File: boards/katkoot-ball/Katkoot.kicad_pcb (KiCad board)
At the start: 2 copper layers, 77.4 x 81.7 mm, 29 parts, among them SW1 Rotary_Encoder_Switch, SW2 SW_Push, SW3 SW_Push, SW5 SW_Push, SW6 SW_Push, SW8 SW_Push, U1 TCR2EF19,LM(CT, U2 PMW3360DM-T2QU, U3 xiao-ble

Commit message: katkoot
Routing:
- net ENC_R: track 101.1 -> 99.7 mm
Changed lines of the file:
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@@
   (segment (start 186.795 39.345) (end 185.23 37.78) (width 0.25) (layer "F.Cu") (net 18))
   (segment (start 187.3 98.85) (end 186.795 98.345) (width 0.25) (layer "F.Cu") (net 18))
-  (segment (start 200.475 107.748833) (end 200.475 106.651167) (width 0.25) (layer "F.Cu") (net 19))
-  (segment (start 199.4 110.95) (end 201.75 108.6) (width 0.25) (layer "F.Cu") (net 19))
-  (segment (start 201.75 108.525) (end 201.251167 108.525) (width 0.25) (layer "F.Cu") (net 19))
-  (segment (start 200.475 106.651167) (end 201.75 105.376167) (width 0.25) (layer "F.Cu") (net 19))
-  (segment (start 201.251167 108.525) (end 200.475 107.748833) (width 0.25) (layer "F.Cu") (net 19))
+  (segment (start 201.75 104.5) (end 201.75 56.9) (width 0.25) (layer "F.Cu") (net 19))
+  (segment (start 199.4 110.95) (end 199.45 110.9) (width 0.25) (layer "F.Cu") (net 19))
+  (segment (start 199.45 110.9) (end 199.45 106.8) (width 0.25) (layer "F.Cu") (net 19))
   (segment (start 189.15 40.55) (end 189.1 40.5) (width 0.25) (layer "F.Cu") (net 19))
   (segment (start 189.15 55.3) (end 189.15 40.55) (width 0.25) (layer "F.Cu") (net 19))
-  (segment (start 201.75 105.376167) (end 201.75 56.9) (width 0.25) (layer "F.Cu") (net 19))
-  (segment (start 201.75 108.6) (end 201.75 108.525) (width 0.25) (layer "F.Cu") (net 19))
+  (segment (start 199.45 106.8) (end 201.75 104.5) (width 0.25) (layer "F.Cu") (net 19))
   (segment (start 201.75 56.9) (end 200.1 55.25) (width 0.25) (layer "F.Cu") (net 19))
   (via (at 199.4 110.95) (size 0.8) (drill 0.4) (layers "F.Cu" "B.Cu") (net 19))

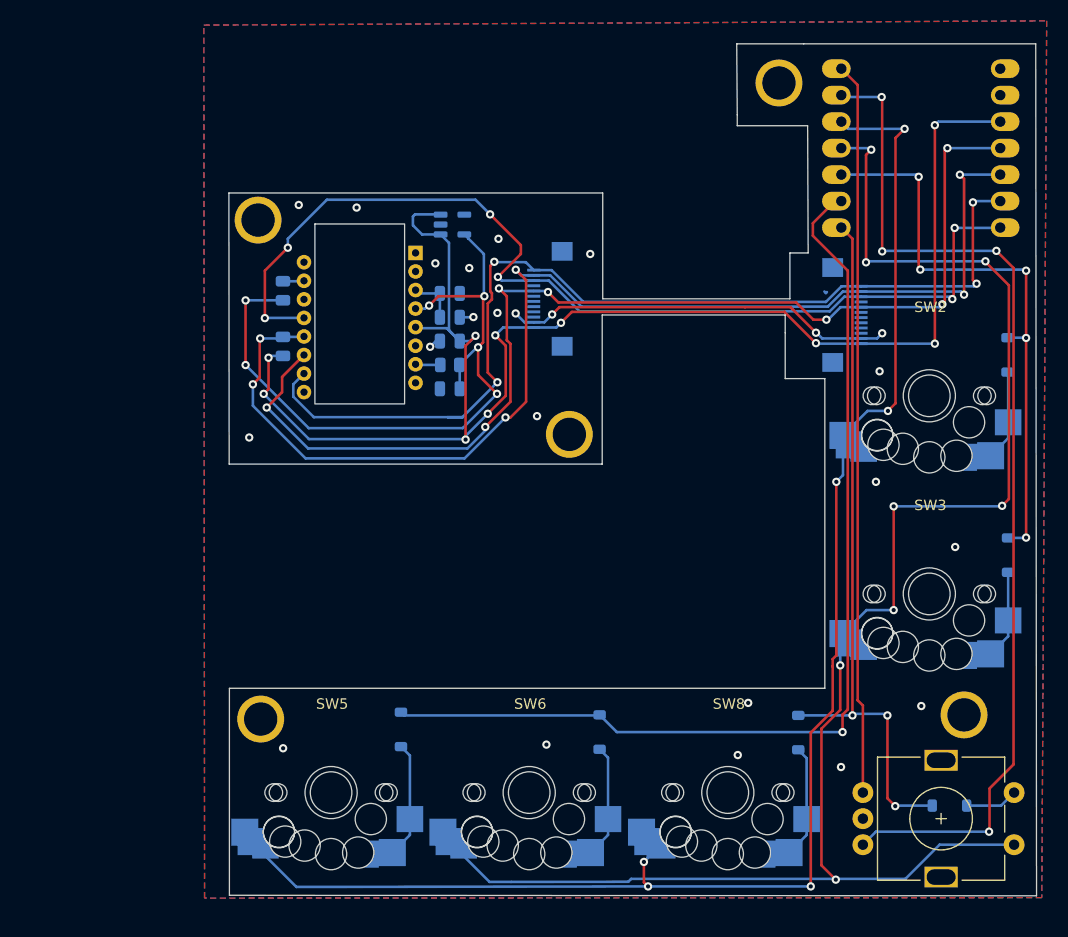
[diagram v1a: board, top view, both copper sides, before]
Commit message: move katkoot keys 1 key to the left
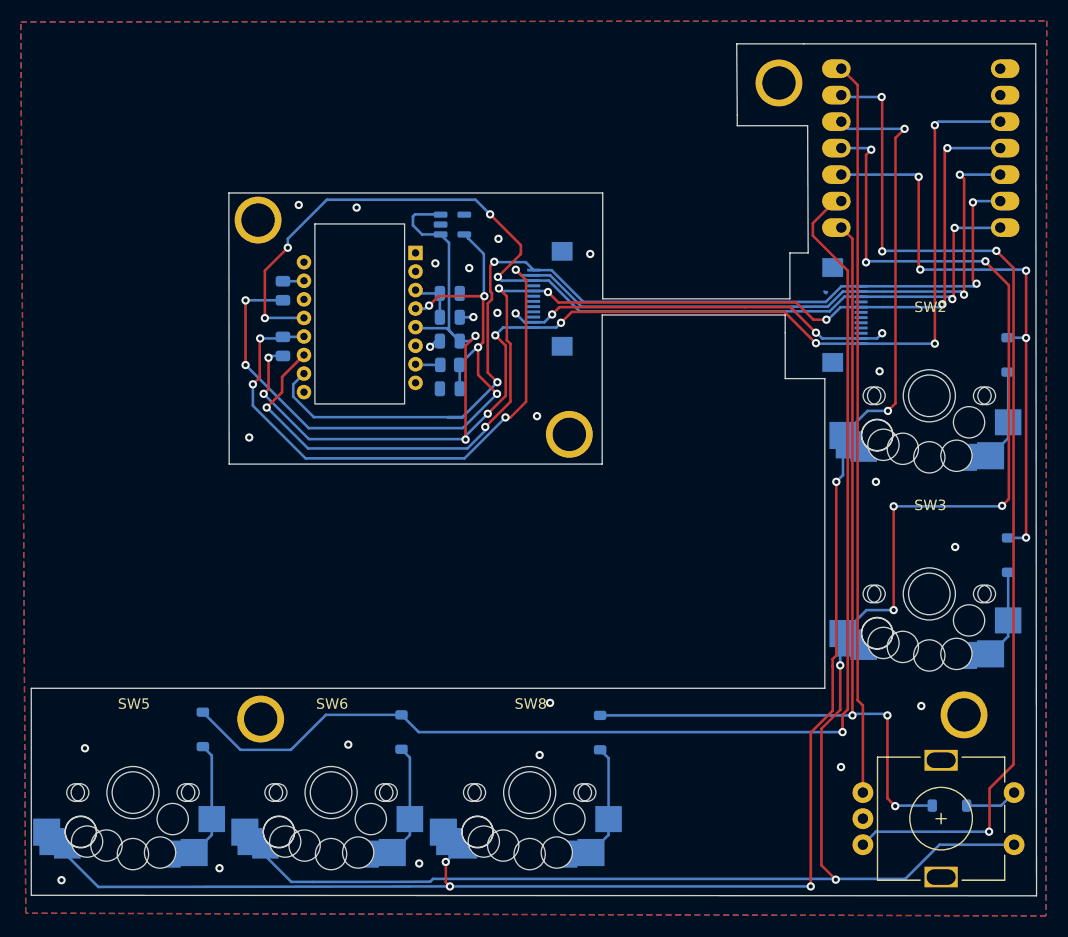
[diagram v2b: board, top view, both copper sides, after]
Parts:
- moved ? 19.0 mm to (110.5, 100.2)
- moved D4 19.0 mm to (124.0, 101.1)
- moved SW5 19.0 mm to (117.3, 107.2)
- moved D5 19.0 mm to (143.1, 101.4)
- moved D7 19.0 mm to (162.1, 101.4)
- moved SW6 19.0 mm to (136.3, 107.2)
- moved SW8 19.0 mm to (155.3, 107.2)
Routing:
- net col1: track 97.2 -> 118.9 mm
- net row_1: track 158.7 -> 177.7 mm
- net row_0: track 144.0 -> 163.0 mm
- net col2: track 68.5 -> 87.5 mm
- net GND: vias 24 -> 27
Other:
- board size 77.4 x 81.7 mm -> 96.4 x 81.7 mm
